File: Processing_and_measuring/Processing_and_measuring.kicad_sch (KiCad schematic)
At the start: 20 parts, among them J1 Conn_01x16_Pin, J2 Conn_01x02_Pin, U1 ATmega64A-A, U2 CD74HC4067M

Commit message: JacobIsTheGOATTTT
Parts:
- removed J1: Conn_01x16_Pin, symbol Connector:Conn_01x16_Pin
- removed U1: ATmega64A-A, Package_QFP:TQFP-64_14x14mm_P0.8mm, symbol MCU_Microchip_ATmega:ATmega64A-A
- added C1, C2: 100n, symbol Device:C
- added J3, J4: Conn_01x07_Pin, symbol Connector:Conn_01x07_Pin
- added L1: 10u, symbol Device:L
- added U1, U4: TPL7407LAD, Package_SO:SOIC-16_3.9x9.9mm_P1.27mm, symbol Transistor_Array:TPL7407LAD
- added U3: AVR128DA48x-xPT, Package_QFP:TQFP-48_7x7mm_P0.5mm, symbol MCU_Microchip_AVR_Dx:AVR128DA48x-xPT
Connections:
- net 5V: now also C2.2, L1.2, U3.28 (AVDD)
- net GND: now also J2.2 (Pin_2), C1.1, C2.1, U1.8 (GND), U3.15 (GND), U3.29 (GND), U3.43 (GND)
- net Read: now also U3.30 (PE0)
- net Power: now reaches J2.1 (Pin_1)
- net Power: now also U1.9 (COM), U4.9 (COM)
- net S0 renamed DOUT1
- net DOUT1: now also U3.37 (PF3)
- net S1 renamed DOUT2
- net DOUT2: now also U3.38 (PF4)
- net S2 renamed DOUT3
- net DOUT3: now also U3.39 (PF5)
- net S3 renamed DOUT4
- net DOUT4: now also U3.40 (~{RESET}/PF6)
- new net: C1.2, L1.1, U3.14 (VDD), U3.42 (VDD)
- new net: J4.7 (Pin_7), U4.10 (OUT7)
- new net: J4.6 (Pin_6), U4.11 (OUT6)
- new net: J4.5 (Pin_5), U4.12 (OUT5)
- new net: J4.4 (Pin_4), U4.13 (OUT4)
- new net: J4.3 (Pin_3), U4.14 (OUT3)
- new net: J4.2 (Pin_2), U4.15 (OUT2)
- new net: J4.1 (Pin_1), U4.16 (OUT1)
- new net: J3.7 (Pin_7), U1.10 (OUT7)
- new net: J3.6 (Pin_6), U1.11 (OUT6)
- new net: J3.5 (Pin_5), U1.12 (OUT5)
- new net: J3.4 (Pin_4), U1.13 (OUT4)
- new net: J3.3 (Pin_3), U1.14 (OUT3)
- new net: J3.2 (Pin_2), U1.15 (OUT2)
- new net: J3.1 (Pin_1), U1.16 (OUT1)
- new net GNd: U4.8 (GND)
- new net motor1: U1.1 (IN1), U3.45 (PA1)
- new net motor10: U3.6 (PB2), U4.3 (IN3)
- new net motor11: U3.7 (PB3), U4.4 (IN4)
- new net motor12: U3.8 (PB4), U4.5 (IN5)
- new net motor13: U3.9 (PB5), U4.6 (IN6)
- new net motor14: U3.10 (PC0), U4.7 (IN7)
- new net motor2: U1.2 (IN2), U3.46 (PA2)
- new net motor3: U1.3 (IN3), U3.47 (PA3)
- new net motor4: U1.4 (IN4), U3.48 (PA4)
- new net motor5: U1.5 (IN5), U3.1 (PA5)
- new net motor6: U1.6 (IN6), U3.2 (PA6)
- new net motor7: U1.7 (IN7), U3.3 (PA7)
- new net motor8: U3.4 (PB0), U4.1 (IN1)
- new net motor9: U3.5 (PB1), U4.2 (IN2)
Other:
- moved on the sheet: J2, R1, R10, R11, R12, R13, R14, R15, R16, R2, R3, R4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

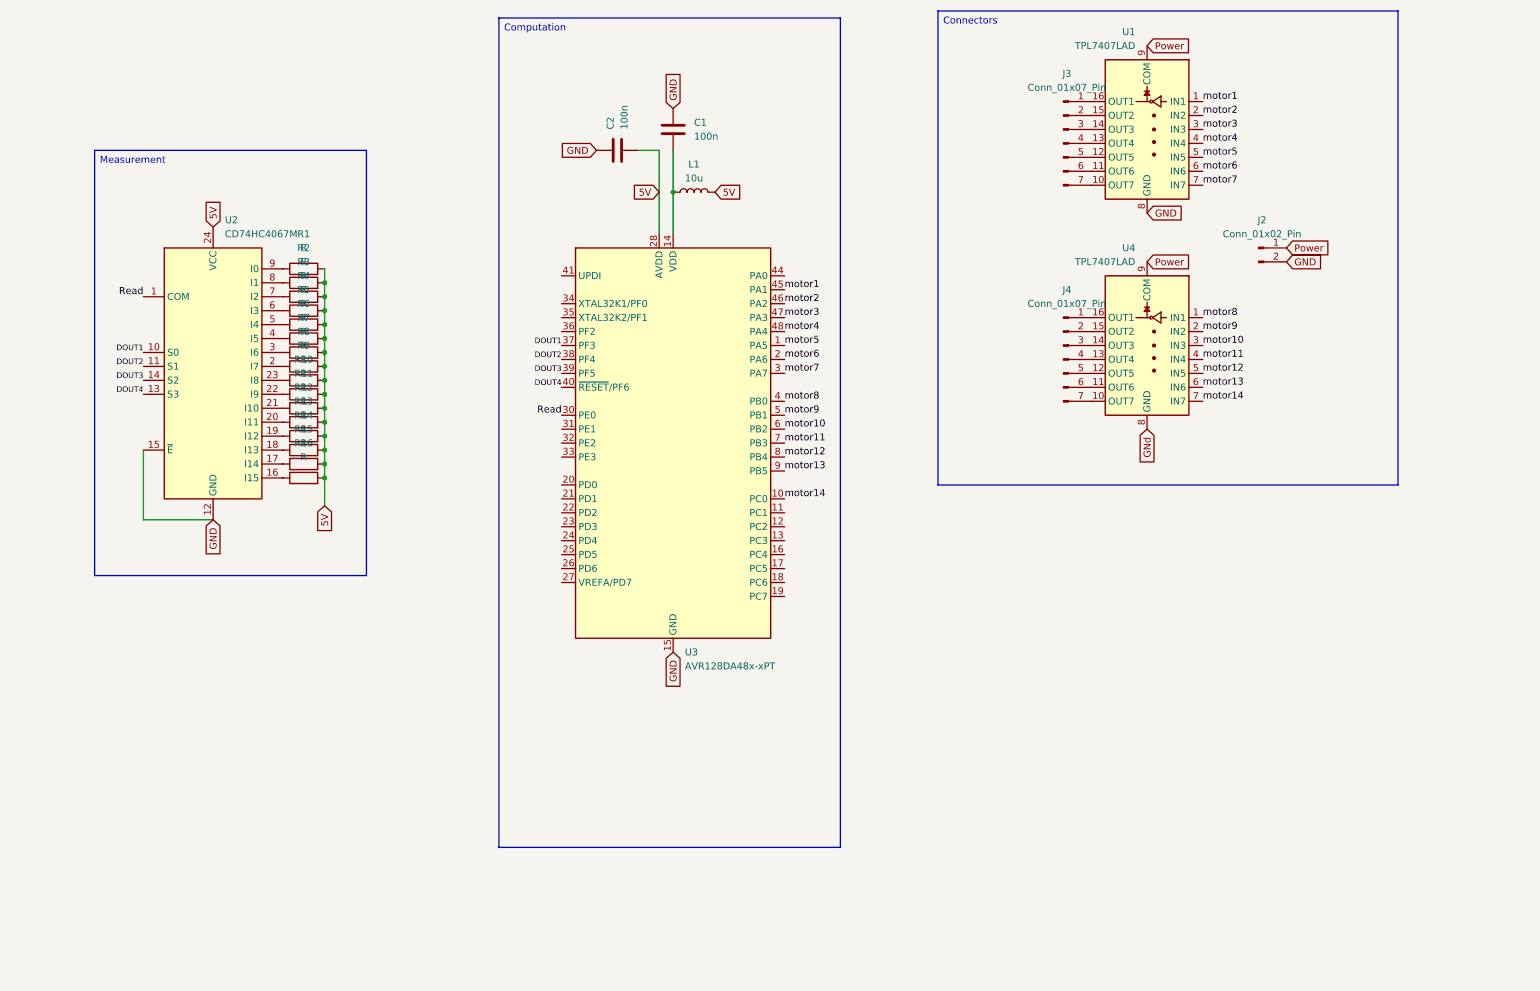
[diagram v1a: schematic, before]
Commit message: added crystal and driver for steppers
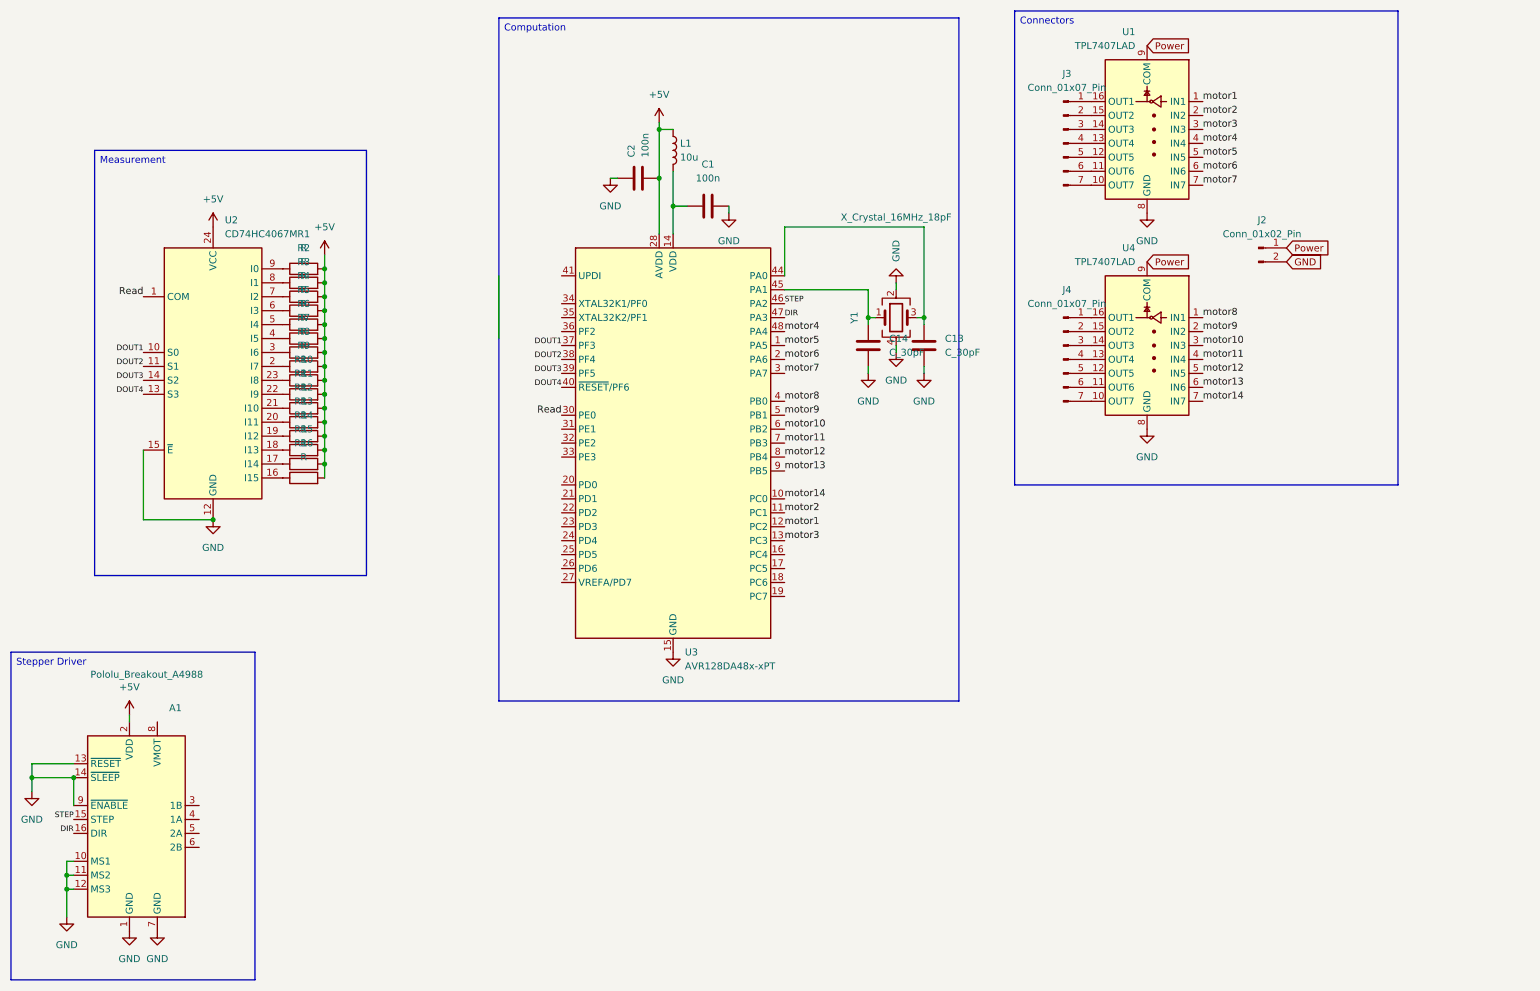
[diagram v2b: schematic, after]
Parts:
- added A1: Pololu_Breakout_A4988, Module:Pololu_Breakout-16_15.2x20.3mm, symbol Driver_Motor:Pololu_Breakout_A4988
- added C13, C14: C_30pF, OEM:C_0603, symbol OEM:C_30pF
- added Y1: X_Crystal_16MHz_18pF, OEM:Crystal_TXC7M, symbol OEM:X_Crystal_16MHz_18pF
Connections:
- net GNd is gone; now on net GND: U4.8 (GND)
- net GND: now also C1.2, A1.1 (GND), A1.10 (MS1), A1.11 (MS2), A1.12 (MS3), A1.13 (~{RESET}), A1.14 (~{SLEEP}), A1.7 (GND), A1.9 (~{ENABLE}), C13.2, C14.2, Y1.2, Y1.4; no longer C1.1
- net motor1: now also U3.12 (PC2); no longer U3.45 (PA1)
- net motor2: now also U3.11 (PC1); no longer U3.46 (PA2)
- net motor3: now also U3.13 (PC3); no longer U3.47 (PA3)
- net at U3.14 (VDD), U3.42 (VDD): now also C1.1, L1.2; no longer C1.2, L1.1
- net at U3.44 (PA0): now also C13.1, Y1.3
- net 5V renamed +5V
- net +5V: now also L1.1, A1.2 (VDD); no longer L1.2
- new net: C14.1, U3.45 (PA1), Y1.1
- new net DIR: A1.16 (DIR), U3.47 (PA3)
- new net STEP: A1.15 (STEP), U3.46 (PA2)
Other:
- moved on the sheet: C1, C2, L1

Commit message: Added footprints and connectors
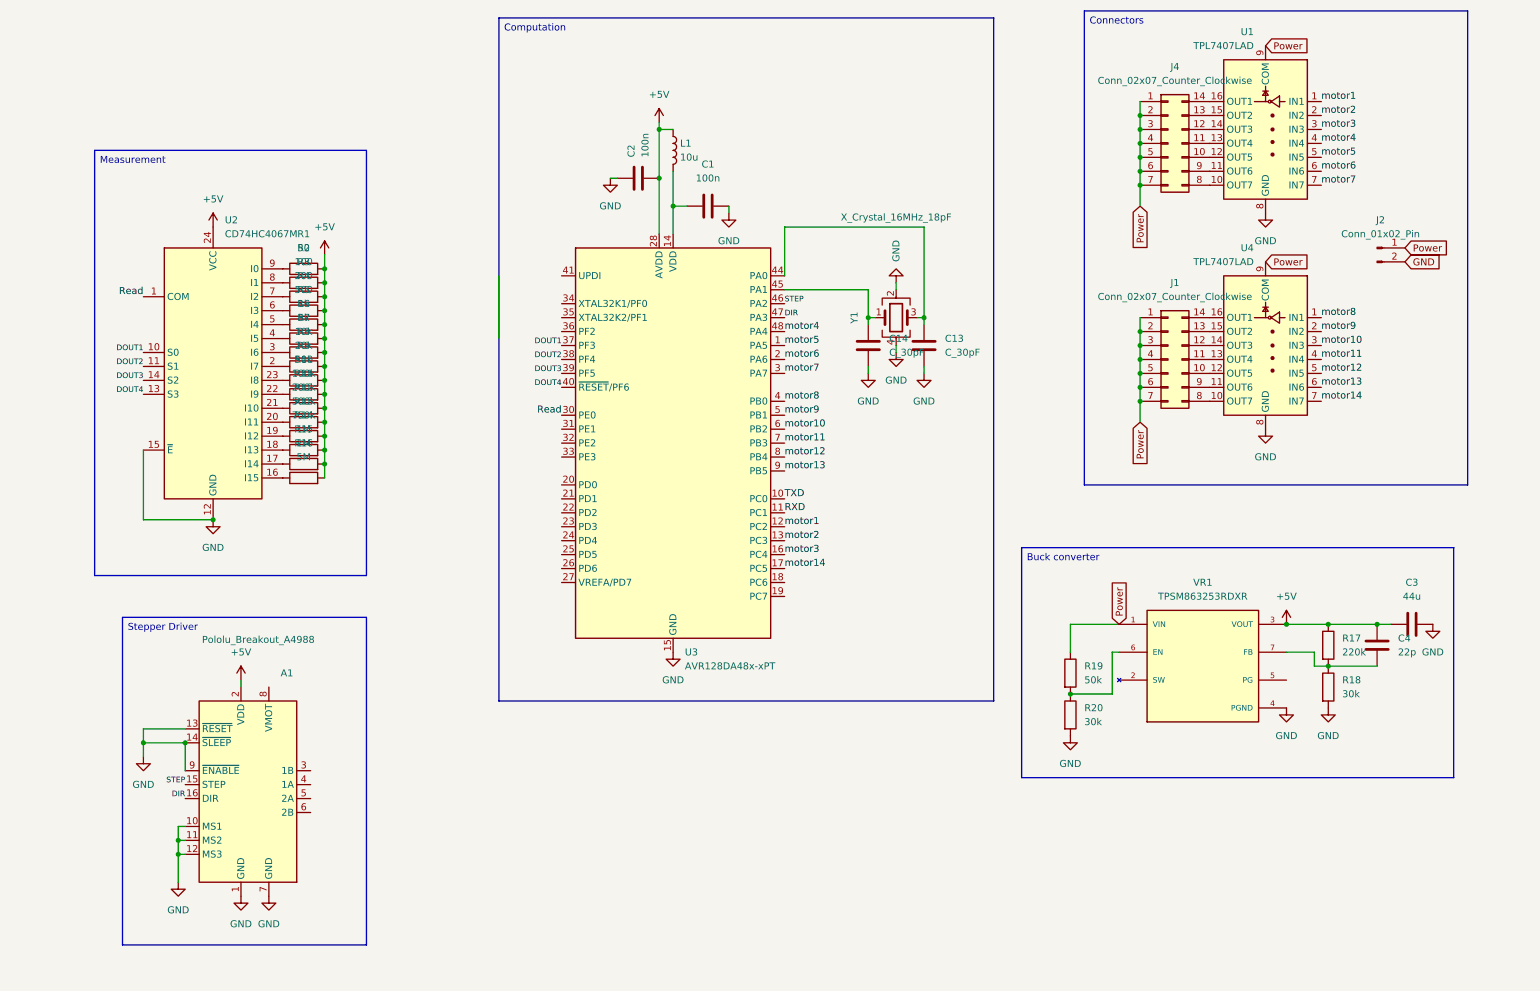
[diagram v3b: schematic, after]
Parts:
- removed J3, J4: Conn_01x07_Pin, symbol Connector:Conn_01x07_Pin
- added C3: 44u, Capacitor_SMD:C_0603_1608Metric, symbol Device:C
- added C4: 22p, Capacitor_SMD:C_0603_1608Metric, symbol Device:C
- added J1, J4: Conn_02x07_Counter_Clockwise, Connector_PinHeader_1.00mm:PinHeader_2x07_P1.00mm_Horizontal, symbol Connector_Generic:Conn_02x07_Counter_Clockwise
- added R17: 220k, Capacitor_SMD:C_0603_1608Metric, symbol Device:R
- added R18, R20: 30k, Capacitor_SMD:C_0603_1608Metric, symbol Device:R
- added R19: 50k, Capacitor_SMD:C_0603_1608Metric, symbol Device:R
- added VR1: TPSM863253RDXR, TPSM863253RDXR:VREG_TPSM863253RDXR, symbol TPSM863253RDXR:TPSM863253RDXR
- C1, C2, L1: footprint (none) -> Capacitor_SMD:C_0603_1608Metric
- C13, C14: footprint OEM:C_0603 -> Capacitor_SMD:C_0603_1608Metric
- J2: footprint (none) -> Connector_AMASS:AMASS_XT60IPW-M_1x03_P7.20mm_Horizontal
- R1: value R -> 50; footprint (none) -> Capacitor_SMD:C_0603_1608Metric
- R10: value R -> 100k; footprint (none) -> Capacitor_SMD:C_0603_1608Metric
- R11: value R -> 200k; footprint (none) -> Capacitor_SMD:C_0603_1608Metric
- R12: value R -> 500k; footprint (none) -> Capacitor_SMD:C_0603_1608Metric
- R13: value R -> 750k; footprint (none) -> Capacitor_SMD:C_0603_1608Metric
- R14: value R -> 1M; footprint (none) -> Capacitor_SMD:C_0603_1608Metric
- R15: value R -> 2M; footprint (none) -> Capacitor_SMD:C_0603_1608Metric
- R16: value R -> 5M; footprint (none) -> Capacitor_SMD:C_0603_1608Metric
- R2: value R -> 100; footprint (none) -> Capacitor_SMD:C_0603_1608Metric
- R3: value R -> 200; footprint (none) -> Capacitor_SMD:C_0603_1608Metric
- R4: value R -> 500; footprint (none) -> Capacitor_SMD:C_0603_1608Metric
- R5: value R -> 1k; footprint (none) -> Capacitor_SMD:C_0603_1608Metric
- R6: value R -> 5k; footprint (none) -> Capacitor_SMD:C_0603_1608Metric
- R7: value R -> 10k; footprint (none) -> Capacitor_SMD:C_0603_1608Metric
- R8: value R -> 20k; footprint (none) -> Capacitor_SMD:C_0603_1608Metric
- R9: value R -> 50k; footprint (none) -> Capacitor_SMD:C_0603_1608Metric
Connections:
- net +5V: now also C3.1, C4.1, R17.1, VR1.3 (VOUT)
- net GND: now also C3.2, R18.2, R20.2, VR1.4 (PGND)
- net Power: now also J1.1 (Pin_1), J1.2 (Pin_2), J1.3 (Pin_3), J1.4 (Pin_4), J1.5 (Pin_5), J1.6 (Pin_6), J1.7 (Pin_7), J4.1 (Pin_1), J4.2 (Pin_2), J4.3 (Pin_3), J4.4 (Pin_4), J4.5 (Pin_5), J4.6 (Pin_6), J4.7 (Pin_7), R19.1, VR1.1 (VIN)
- net motor14: now also U3.17 (PC5); no longer U3.10 (PC0)
- net motor2: now also U3.13 (PC3); no longer U3.11 (PC1)
- net motor3: now also U3.16 (PC4); no longer U3.13 (PC3)
- net at U4.10 (OUT7): now also J1.8 (Pin_8)
- net at U4.11 (OUT6): now also J1.9 (Pin_9)
- net at U4.12 (OUT5): now also J1.10 (Pin_10)
- net at U4.13 (OUT4): now also J1.11 (Pin_11)
- net at U4.14 (OUT3): now also J1.12 (Pin_12)
- net at U4.15 (OUT2): now also J1.13 (Pin_13)
- net at U4.16 (OUT1): now also J1.14 (Pin_14)
- net at U1.10 (OUT7): now also J4.8 (Pin_8)
- net at U1.11 (OUT6): now also J4.9 (Pin_9)
- net at U1.12 (OUT5): now also J4.10 (Pin_10)
- net at U1.13 (OUT4): now also J4.11 (Pin_11)
- net at U1.14 (OUT3): now also J4.12 (Pin_12)
- net at U1.15 (OUT2): now also J4.13 (Pin_13)
- net at U1.16 (OUT1): now also J4.14 (Pin_14)
- new net: R19.2, R20.1, VR1.6 (EN)
- new net: C4.2, R17.2, R18.1, VR1.7 (FB)
- new net RXD: U3.11 (PC1)
- new net TXD: U3.10 (PC0)
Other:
- moved on the sheet: A1, J2, U1, U4

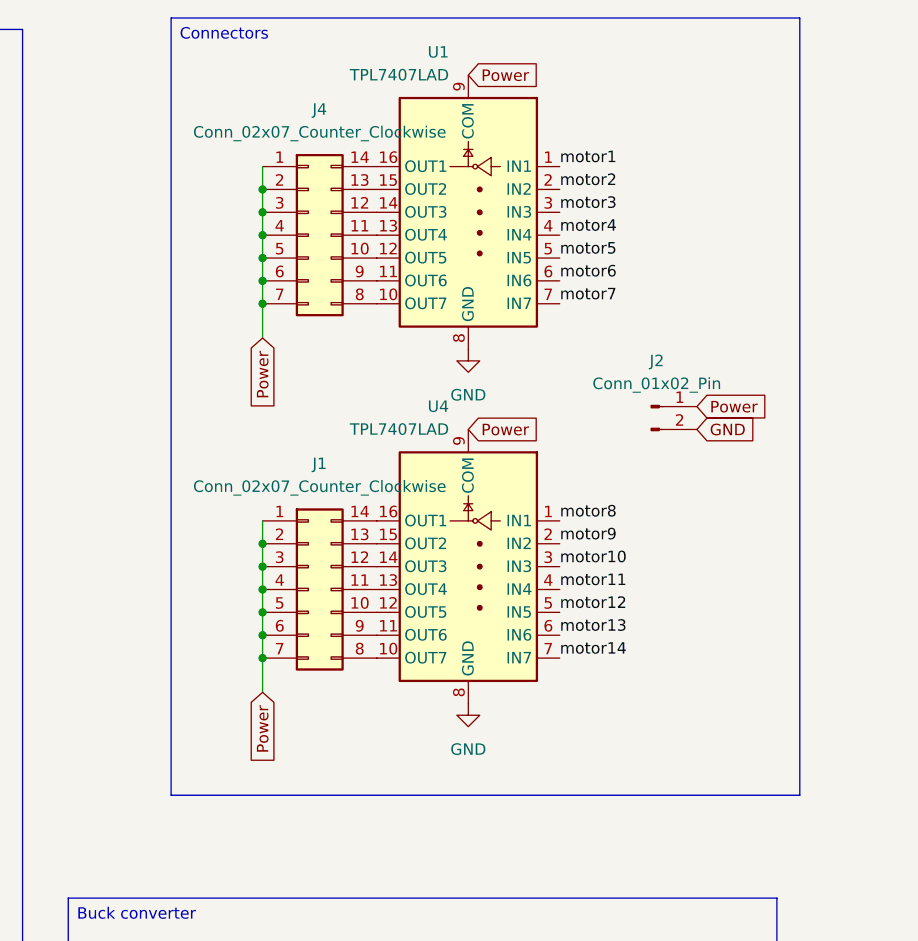
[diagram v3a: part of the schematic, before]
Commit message: Started layout
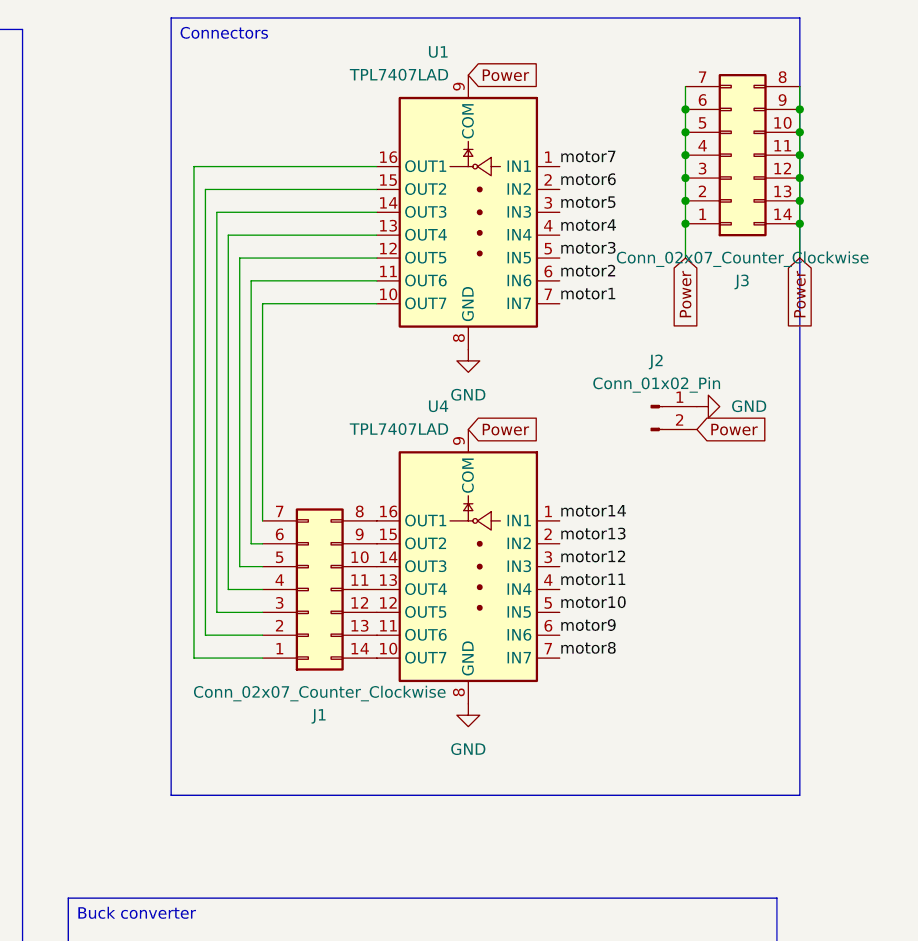
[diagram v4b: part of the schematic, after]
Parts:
- removed J4: Conn_02x07_Counter_Clockwise, Connector_PinHeader_1.00mm:PinHeader_2x07_P1.00mm_Horizontal, symbol Connector_Generic:Conn_02x07_Counter_Clockwise
- added J3: Conn_02x07_Counter_Clockwise, Connector_PinHeader_1.00mm:PinHeader_2x07_P1.00mm_Horizontal, symbol Connector_Generic:Conn_02x07_Counter_Clockwise
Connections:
- net GND: now also J2.1 (Pin_1); no longer J2.2 (Pin_2)
- net Power: now also J2.2 (Pin_2), J3.1 (Pin_1), J3.10 (Pin_10), J3.11 (Pin_11), J3.12 (Pin_12), J3.13 (Pin_13), J3.14 (Pin_14), J3.2 (Pin_2), J3.3 (Pin_3), J3.4 (Pin_4), J3.5 (Pin_5), J3.6 (Pin_6), J3.7 (Pin_7), J3.8 (Pin_8), J3.9 (Pin_9); no longer J1.1 (Pin_1), J1.2 (Pin_2), J1.3 (Pin_3), J1.4 (Pin_4), J1.5 (Pin_5), J1.6 (Pin_6), J1.7 (Pin_7), J2.1 (Pin_1)
- net motor1: now also U1.7 (IN7); no longer U1.1 (IN1)
- net motor10: now also U4.5 (IN5); no longer U4.3 (IN3)
- net motor12: now also U4.3 (IN3); no longer U4.5 (IN5)
- net motor13: now also U4.2 (IN2); no longer U4.6 (IN6)
- net motor14: now also U4.1 (IN1); no longer U4.7 (IN7)
- net motor2: now also U1.6 (IN6); no longer U1.2 (IN2)
- net motor3: now also U1.5 (IN5); no longer U1.3 (IN3)
- net motor5: now also U1.3 (IN3); no longer U1.5 (IN5)
- net motor6: now also U1.2 (IN2); no longer U1.6 (IN6)
- net motor7: now also U1.1 (IN1); no longer U1.7 (IN7)
- net motor8: now also U4.7 (IN7); no longer U4.1 (IN1)
- net motor9: now also U4.6 (IN6); no longer U4.2 (IN2)
- net at U1.12 (OUT5): now also J1.5 (Pin_5)
- net at U1.13 (OUT4): now also J1.4 (Pin_4)
- net at U1.14 (OUT3): now also J1.3 (Pin_3)
- net at U1.15 (OUT2): now also J1.2 (Pin_2)
- net at U1.16 (OUT1): now also J1.1 (Pin_1)
- net at U1.10 (OUT7): now also J1.7 (Pin_7)
- net at U1.11 (OUT6): now also J1.6 (Pin_6)
- net at J1.10 (Pin_10): now also U4.14 (OUT3); no longer U4.12 (OUT5)
- net at J1.12 (Pin_12): now also U4.12 (OUT5); no longer U4.14 (OUT3)
- net at J1.13 (Pin_13): now also U4.11 (OUT6); no longer U4.15 (OUT2)
- net at J1.14 (Pin_14): now also U4.10 (OUT7); no longer U4.16 (OUT1)
- net at J1.8 (Pin_8): now also U4.16 (OUT1); no longer U4.10 (OUT7)
- net at J1.9 (Pin_9): now also U4.15 (OUT2); no longer U4.11 (OUT6)
